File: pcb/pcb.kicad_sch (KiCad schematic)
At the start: 29 parts, among them IC1 TPS63802DLAT, IC2 TUSB320LIRWBR, J1 USB_C_Receptacle_PowerOnly_6P, Q1 2N7002, U1 BQ24075RGTR

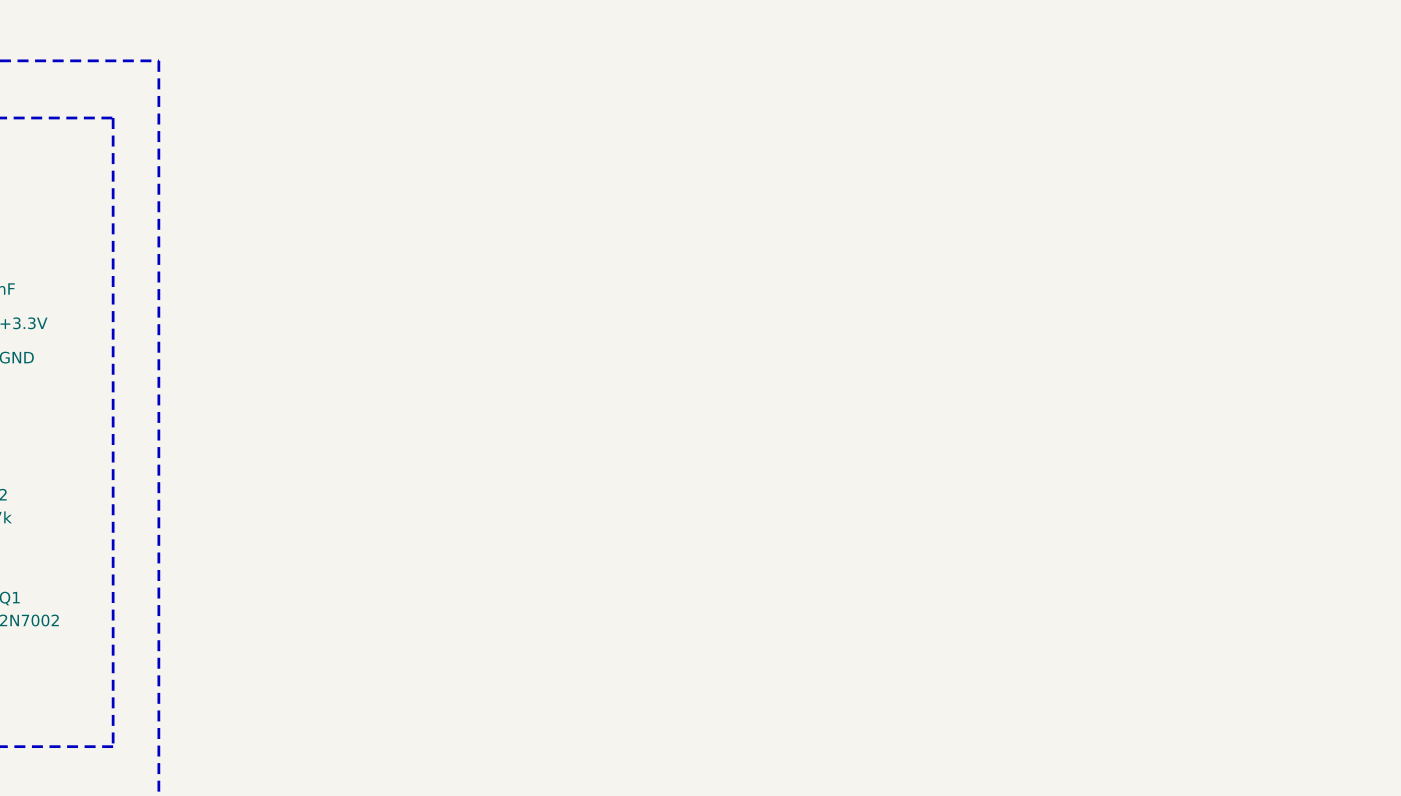
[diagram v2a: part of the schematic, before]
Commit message: Added sensor and actor control using an ESP32
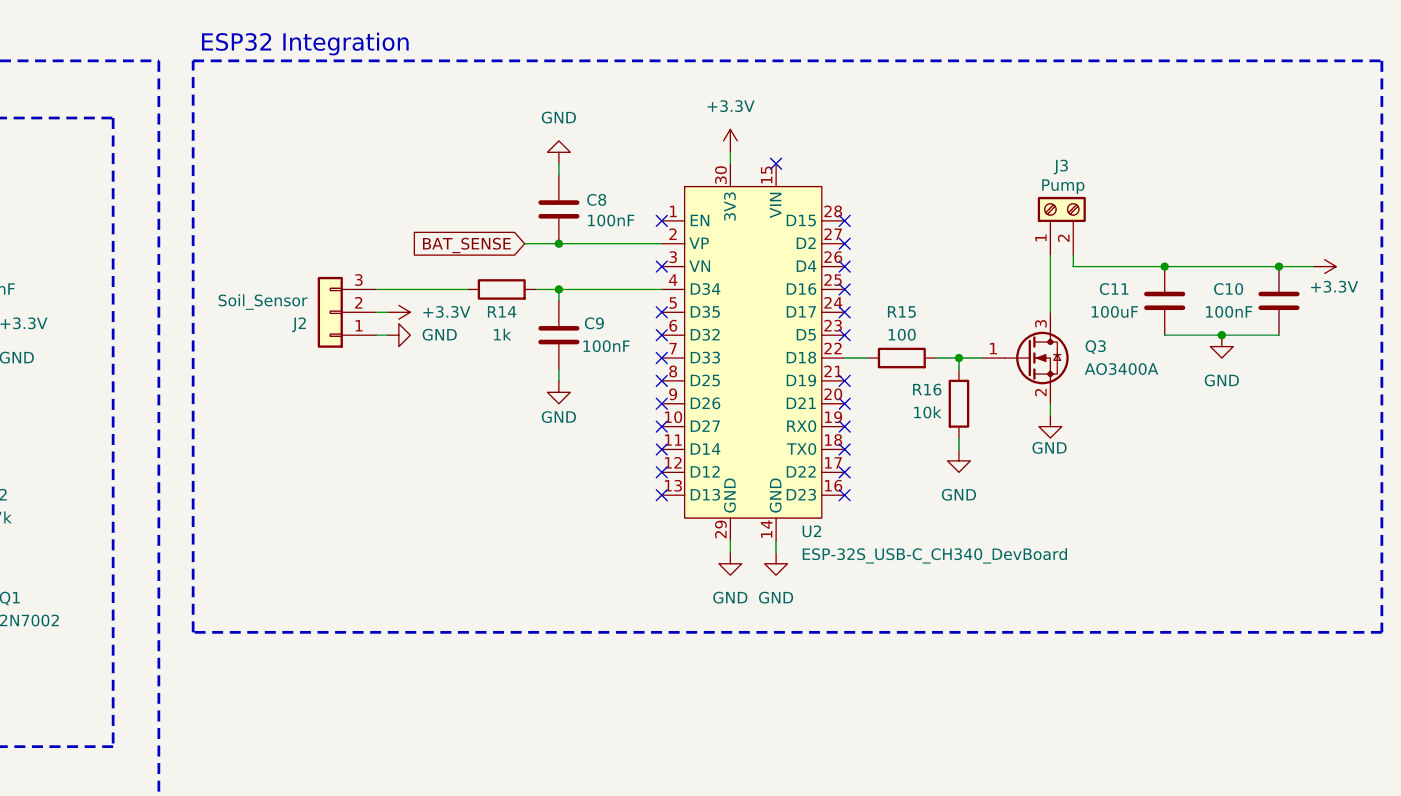
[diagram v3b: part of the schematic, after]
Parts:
- added C10, C8, C9: 100nF, symbol Device:C
- added C11: 100uF, symbol Device:C
- added J2: Soil_Sensor, Connector_PinHeader_2.54mm:PinHeader_1x03_P2.54mm_Vertical, symbol Connector_Generic:Conn_01x03
- added J3: Pump, TerminalBlock_Phoenix:TerminalBlock_Phoenix_MKDS-1,5-2-5.08_1x02_P5.08mm_Horizontal, symbol Connector:Screw_Terminal_01x02
- added Q3: AO3400A, Package_TO_SOT_SMD:SOT-23, symbol Transistor_FET:AO3400A
- added R14: 1k, symbol Device:R
- added R15: 100, symbol Device:R
- added R16: 10k, symbol Device:R
- added U2: ESP-32S_USB-C_CH340_DevBoard, pcb:ESP-32S_USB-C_CH340_DevBoard, symbol pcb:ESP-32S_USB-C_CH340_DevBoard
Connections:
- net +3.3V: now also C10.1, C11.1, J2.2 (Pin_2), J3.2 (Pin_2), U2.30 (3V3)
- net BAT_SENSE: now also C8.1, U2.2 (VP)
- net GND: now also C10.2, C11.2, C8.2, C9.2, J2.1 (Pin_1), Q3.2 (S), R16.2, U2.14 (GND), U2.29 (GND)
- new net: J2.3 (Pin_3), R14.1
- new net: J3.1 (Pin_1), Q3.3 (D)
- new net: Q3.1 (G), R15.2, R16.1
- new net: R15.1, U2.22 (D18)
- new net: C9.1, R14.2, U2.4 (D34)
- no-connect marks 5 -> 29
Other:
- note added: "ESP32 Integration"

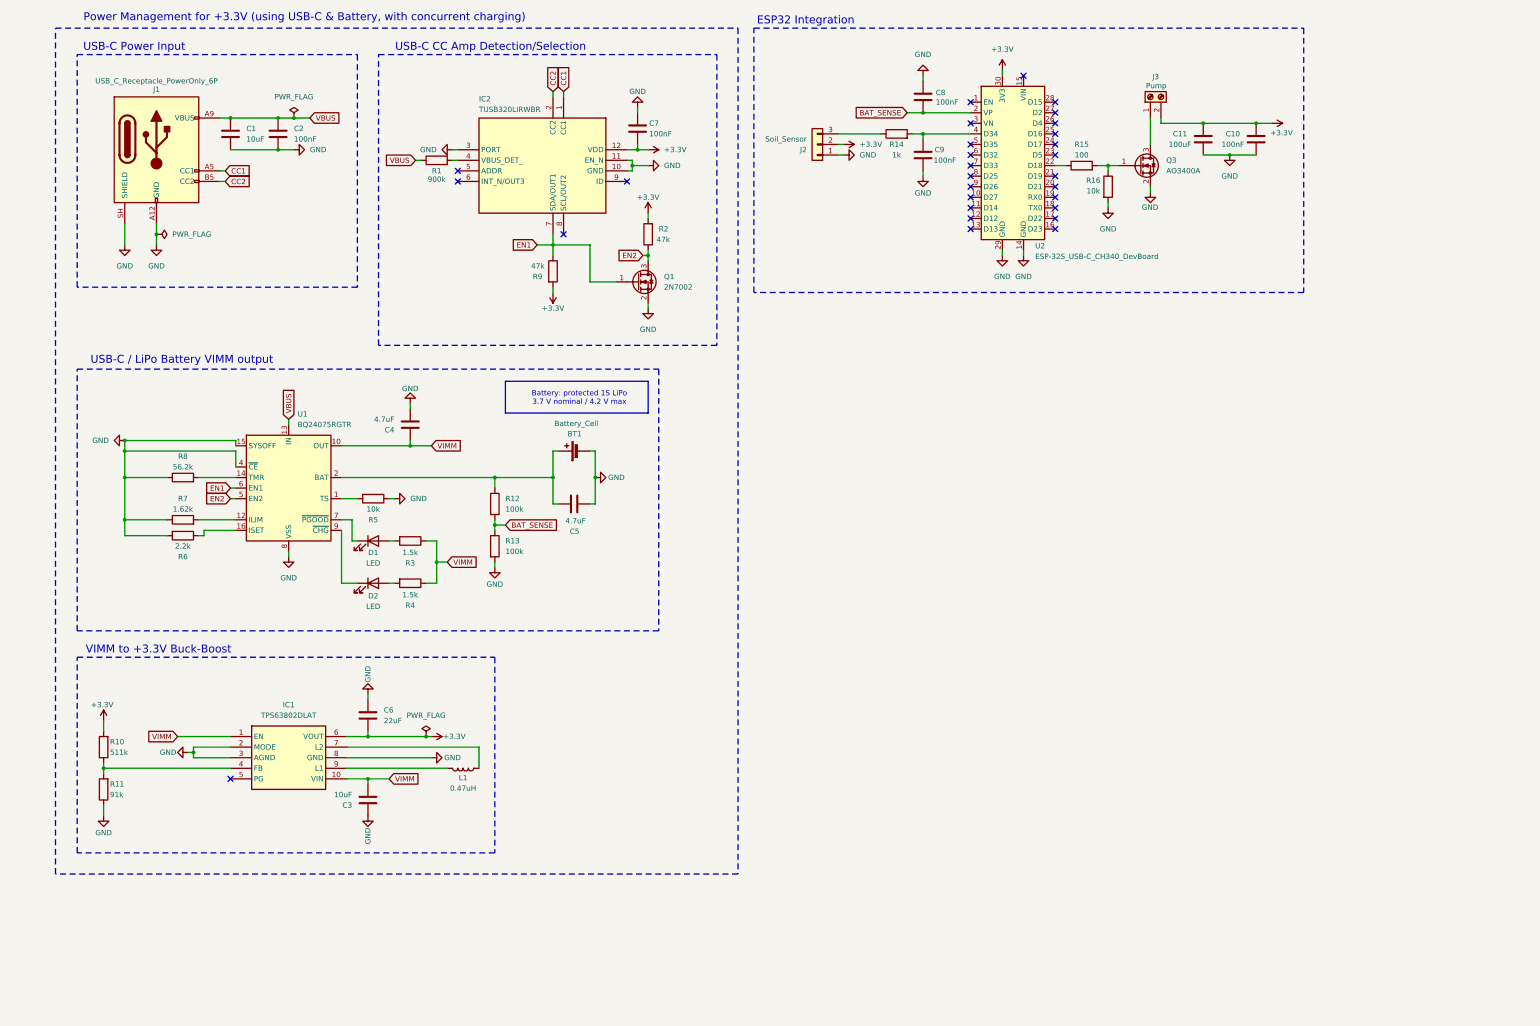
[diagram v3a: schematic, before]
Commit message: Added some USB-C protection & further optimizations to the schematic
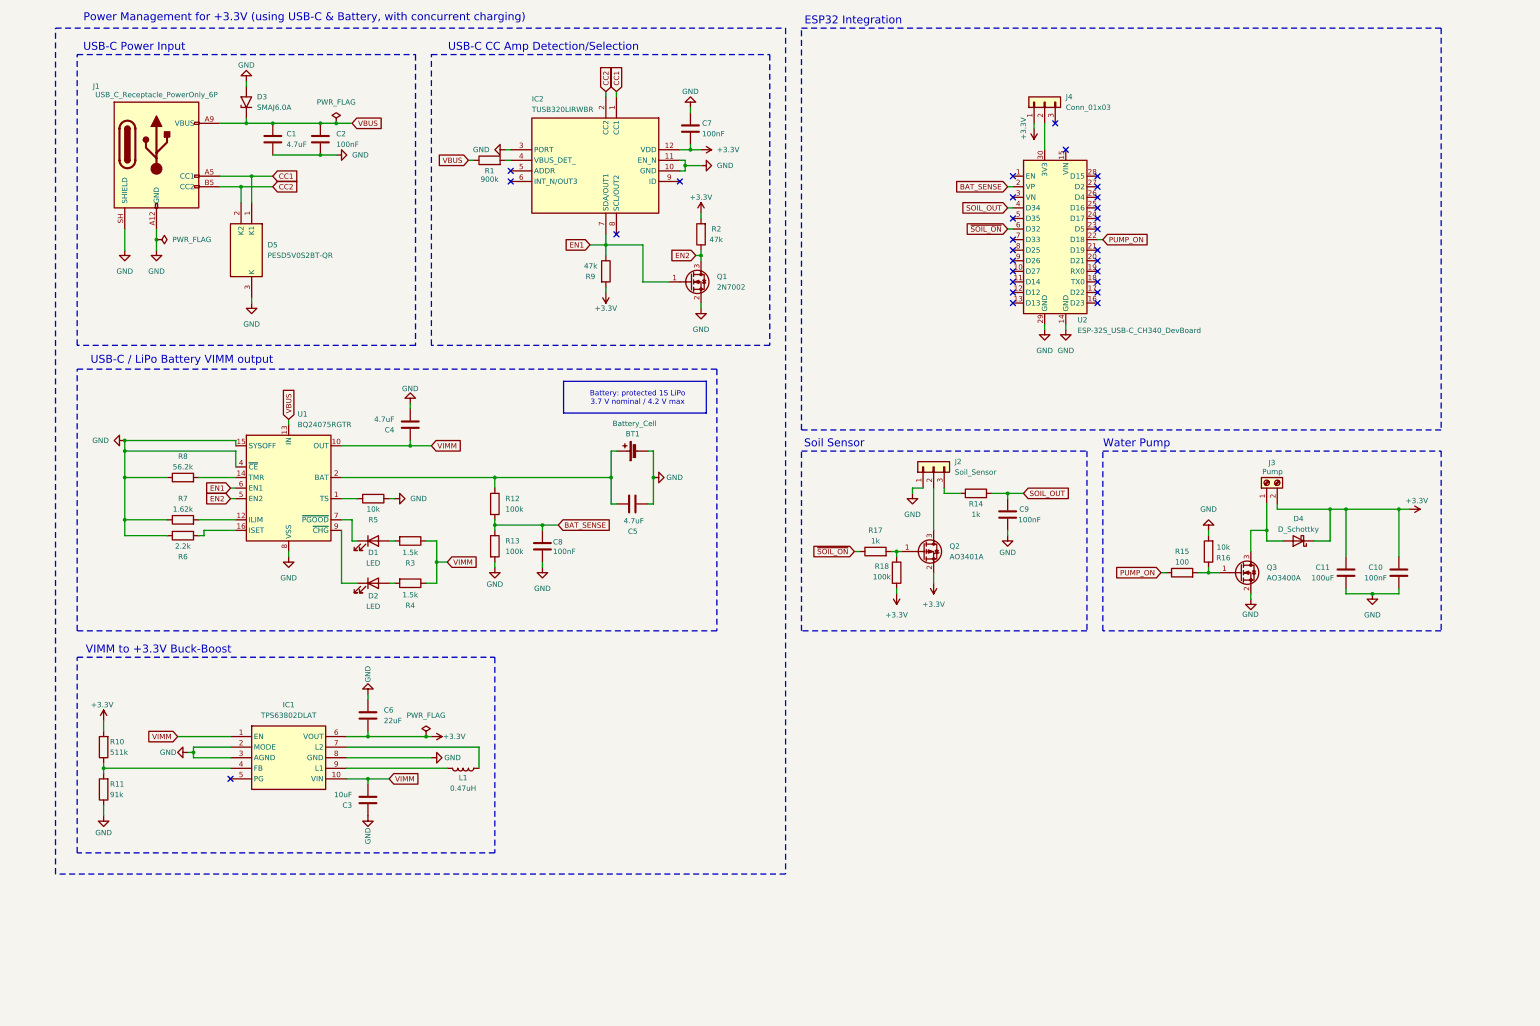
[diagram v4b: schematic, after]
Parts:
- added D3: SMAJ6.0A, Diode_SMD:D_SMA_Handsoldering, symbol Diode:SMAJ6.0A
- added D4: D_Schottky, Diode_SMD:D_SMA_Handsoldering, symbol Device:D_Schottky
- added D5: PESD5V0S2BT-QR, PESD5V0S2BTQR, symbol SamacSys:PESD5V0S2BT-QR
- added J4: Conn_01x03, Connector_PinHeader_1.00mm:PinHeader_1x03_P1.00mm_Vertical, symbol Connector_Generic:Conn_01x03
- added Q2: AO3401A, Package_TO_SOT_SMD:SOT-23, symbol Transistor_FET:AO3401A
- added R17: 1k, Resistor_SMD:R_1206_3216Metric_Pad1.30x1.75mm_HandSolder, symbol Device:R
- added R18: 100k, Resistor_SMD:R_1206_3216Metric_Pad1.30x1.75mm_HandSolder, symbol Device:R
- C1: value 10uF -> 4.7uF; footprint (none) -> Capacitor_SMD:C_1206_3216Metric_Pad1.33x1.80mm_HandSolder
- C10, C11, C2, C3, C4, C5, C6, C7, C8, C9: footprint (none) -> Capacitor_SMD:C_1206_3216Metric_Pad1.33x1.80mm_HandSolder
- D1, D2: footprint (none) -> LED_THT:LED_D4.0mm
- J1: footprint Package_DFN_QFN:Texas_RNQ0040A_WQFN-40-1EP_6x4mm_P0.4mm_EP4.7x2.7mm -> Connector_USB:USB_C_Receptacle_GCT_USB4125-xx-x-0190_6P_TopMnt_Horizontal
- L1: footprint (none) -> Inductor_SMD:L_1206_3216Metric_Pad1.22x1.90mm_HandSolder
- Q1: footprint (none) -> Package_TO_SOT_SMD:SOT-23
- R1, R10, R11, R12, R13, R14, R15, R16, R2, R3, R4, R5, R6, R7, R8, R9: footprint (none) -> Resistor_SMD:R_1206_3216Metric_Pad1.30x1.75mm_HandSolder
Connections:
- net +3.3V: now also D4.1 (K), J4.1 (Pin_1), Q2.2 (S), R18.2; no longer J2.2 (Pin_2), U2.30 (3V3)
- net CC1: now also D5.1 (K1)
- net CC2: now also D5.2 (K2)
- net GND: now also D3.2 (A2), D5.3 (K)
- net VBUS: now also D3.1 (A1)
- net at J3.1 (Pin_1), Q3.3 (D): now also D4.2 (A)
- net PUMP_ON: now reaches R15.1, U2.22 (D18)
- net SOIL_OUT: now reaches C9.1, R14.2, U2.4 (D34)
- net ~{SOIL_ON}: now reaches U2.6 (D32)
- net ~{SOIL_ON}: now also R17.1
- new net: J2.2 (Pin_2), Q2.3 (D)
- new net: Q2.1 (G), R17.2, R18.1
- new net: J4.2 (Pin_2), U2.30 (3V3)
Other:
- note added: "Soil Sensor"
- note added: "Water Pump"
- moved on the sheet: BT1, C1, C2, C5, C7, C9, IC2, J1, J2, Q1, R1, R14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

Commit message: Testing some KiCAD preview (PCB, Schematic) and checks (ERC, DRC) automation
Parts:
- added TP1: VBUS, TestPoint:TestPoint_Pad_D2.0mm, symbol Connector:TestPoint
- added TP10: PUMP_DRAIN, TestPoint:TestPoint_Pad_D2.0mm, symbol Connector:TestPoint
- added TP2: VIMM, TestPoint:TestPoint_Pad_D2.0mm, symbol Connector:TestPoint
- added TP3: BAT, TestPoint:TestPoint_Pad_D2.0mm, symbol Connector:TestPoint
- added TP4: 3.3V, TestPoint:TestPoint_Pad_D2.0mm, symbol Connector:TestPoint
- added TP5: BAT_SENSE, TestPoint:TestPoint_Pad_D2.0mm, symbol Connector:TestPoint
- added TP6: SOIL_OUT, TestPoint:TestPoint_Pad_D2.0mm, symbol Connector:TestPoint
- added TP7: ~{SOIL_ON}, TestPoint:TestPoint_Pad_D2.0mm, symbol Connector:TestPoint
- added TP8: PUMP_ON, TestPoint:TestPoint_Pad_D2.0mm, symbol Connector:TestPoint
- added TP9: SOIL_DRAIN, TestPoint:TestPoint_Pad_D2.0mm, symbol Connector:TestPoint
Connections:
- net +3.3V: now also TP4.1
- net BAT_SENSE: now also TP5.1
- net PUMP_ON: now also TP8.1
- net SOIL_OUT: now also TP6.1
- net VBUS: now also TP1.1
- net VIMM: now also TP2.1
- net ~{SOIL_ON}: now also TP7.1
- net at J2.2 (Pin_2), Q2.3 (D): now also TP9.1
- net at BT1.1 (+), C5.1, R12.1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: now also TP3.1
- net at D4.2 (A), J3.1 (Pin_1), Q3.3 (D): now also TP10.1
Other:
- moved on the sheet: BT1, C10, C11, C5, C9, D4, J2, J3, L1, Q2, Q3, R14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
